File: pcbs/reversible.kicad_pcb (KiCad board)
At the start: 2 copper layers, 132.7 x 86.8 mm, 50 parts

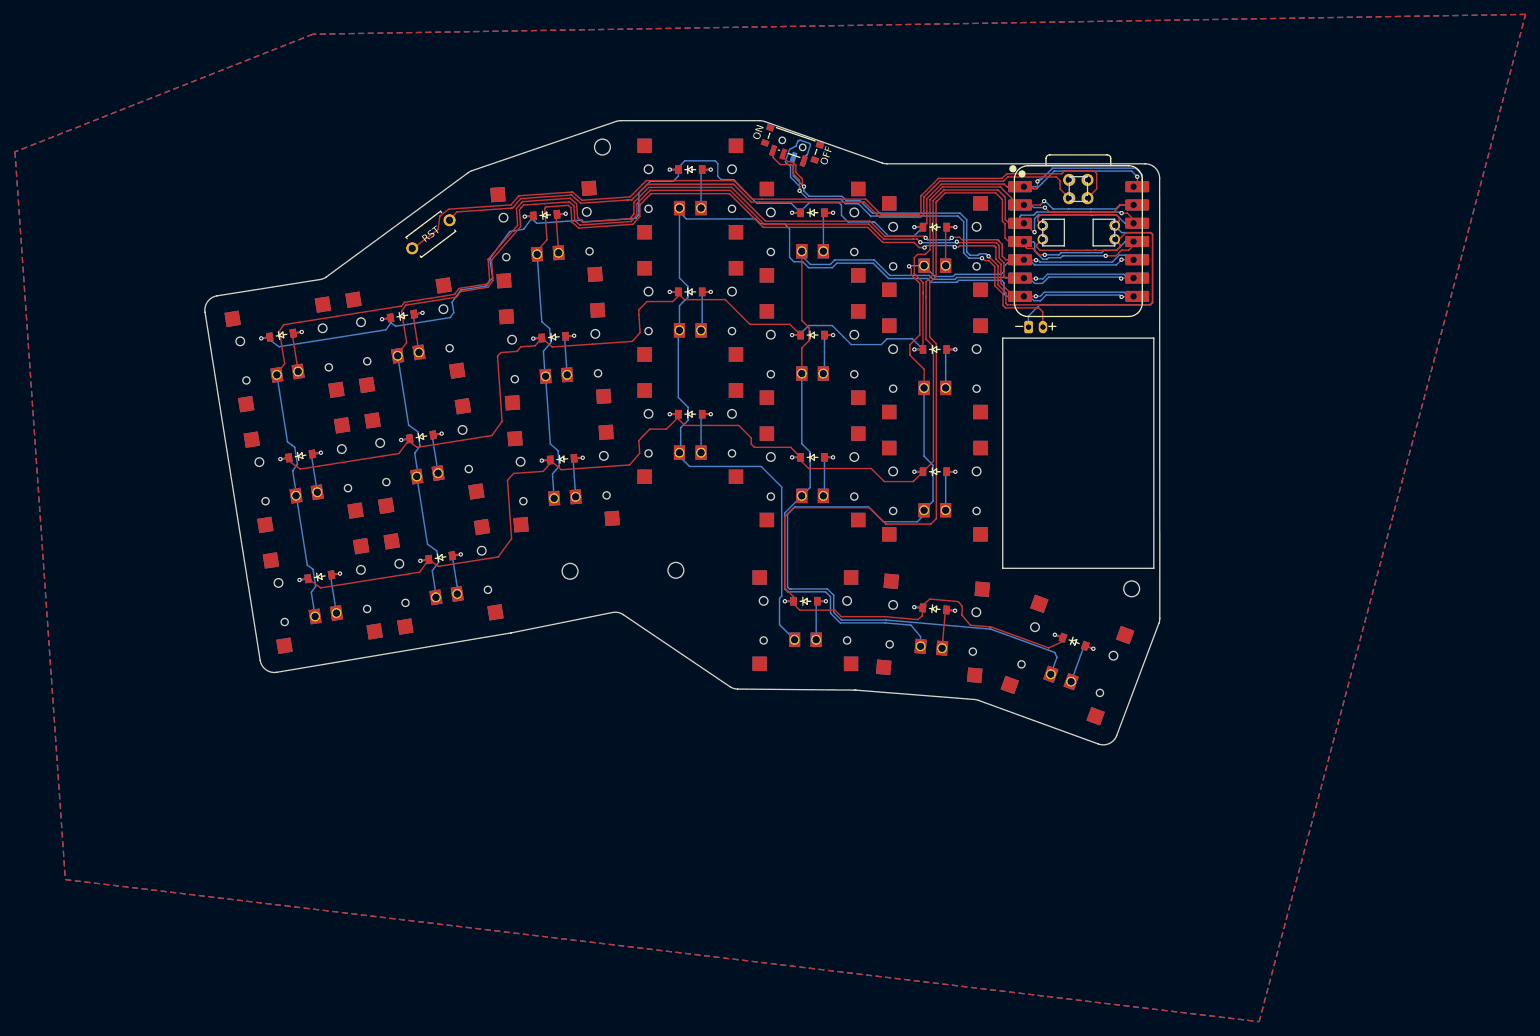
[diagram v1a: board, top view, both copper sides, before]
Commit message: finalized the pcb. cleaned up some tracks. ordered first sample
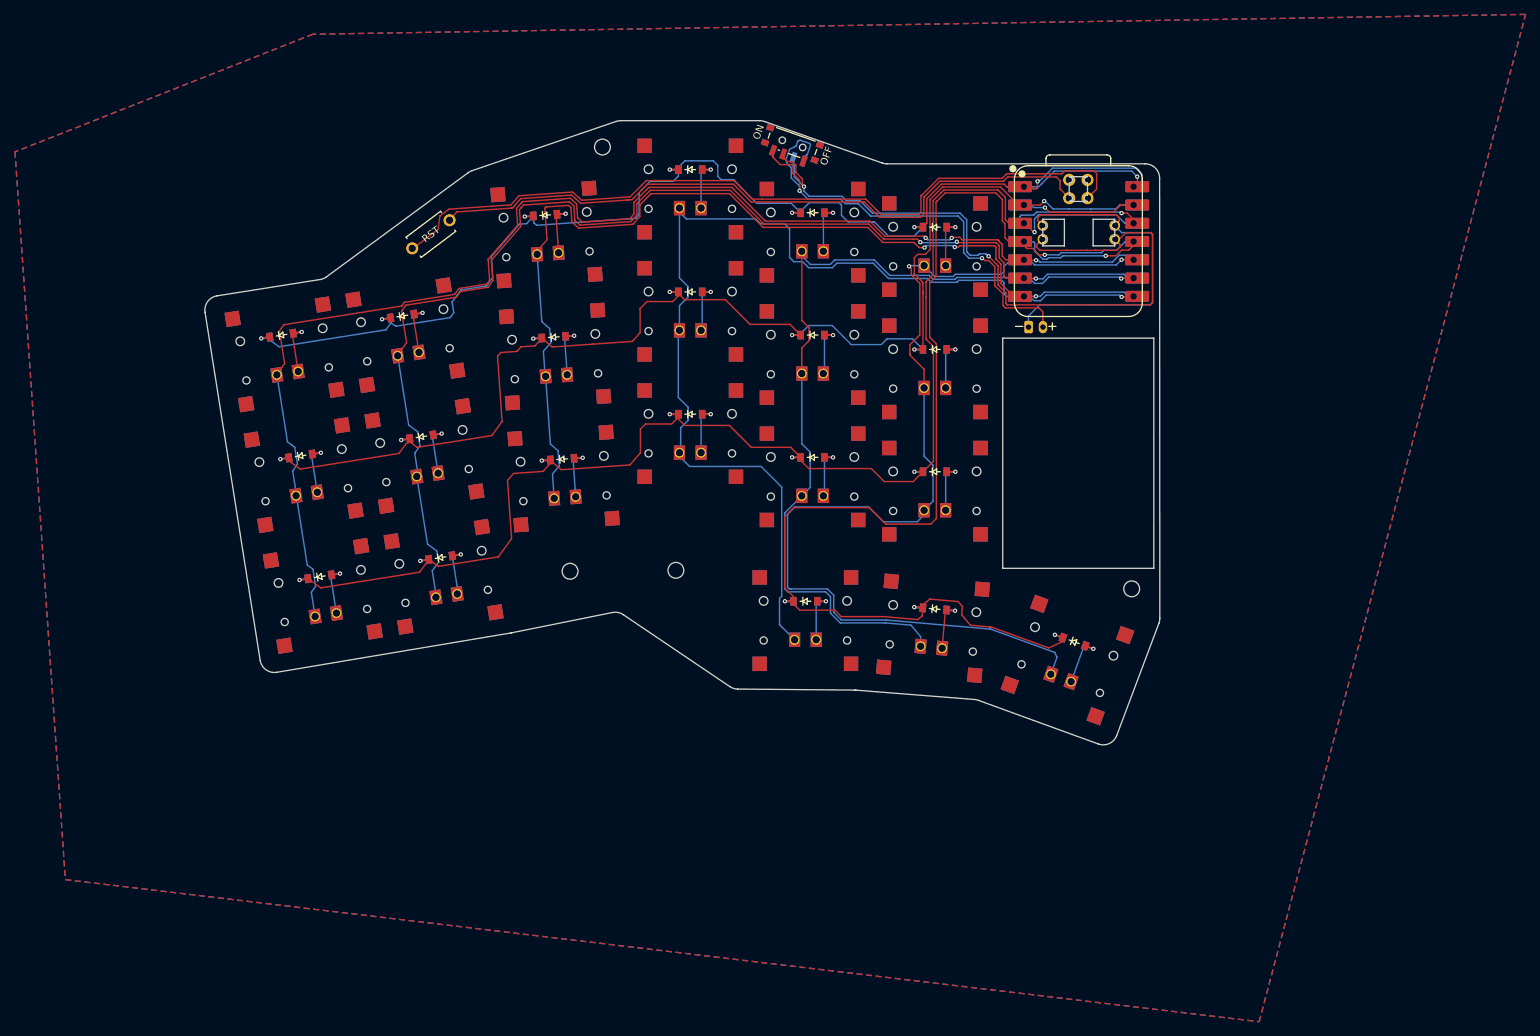
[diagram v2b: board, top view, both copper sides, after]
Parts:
- turned PWR1 to 70.6 degrees
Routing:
- net BAT_P: track 69.5 -> 70.5 mm
- net P9: track 148.0 -> 147.0 mm
- net RAW: track 102.3 -> 103.2 mm

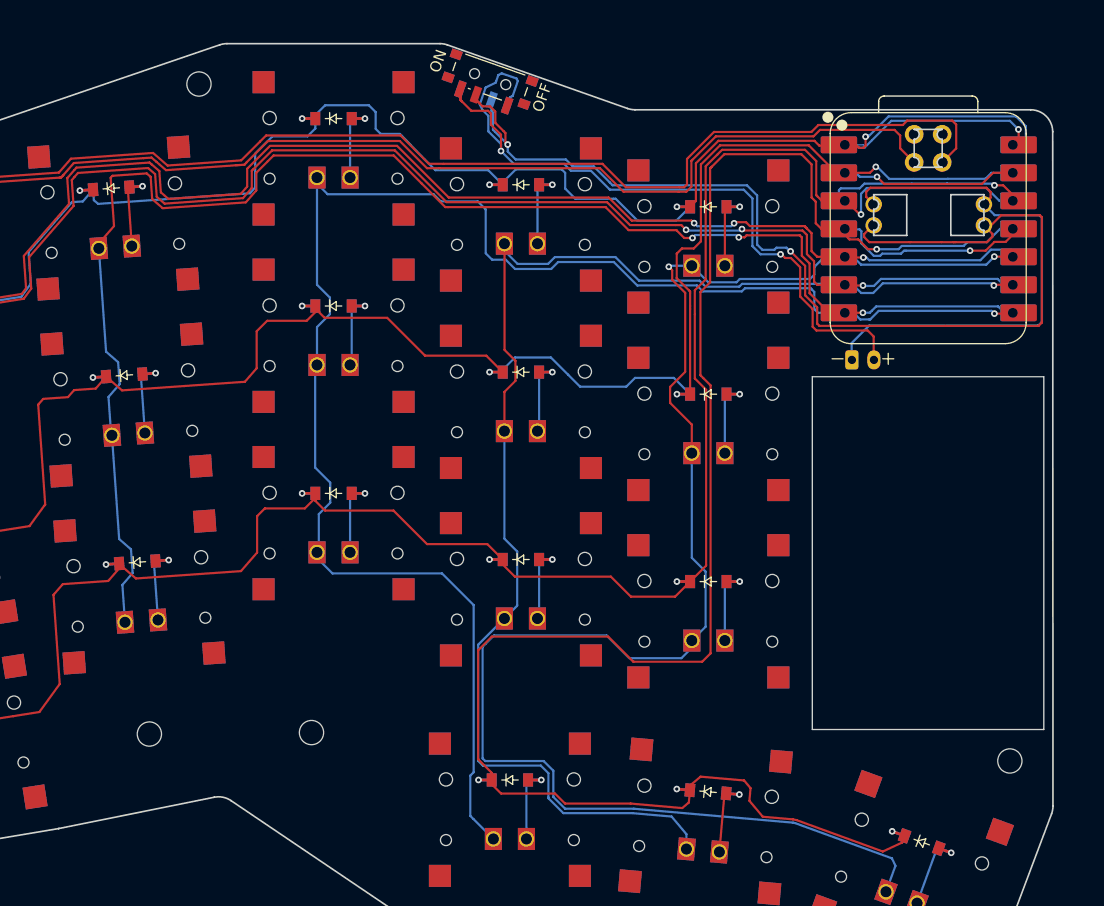
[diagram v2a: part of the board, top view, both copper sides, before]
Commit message: overhauled mcu footprint to meed fab specifications. updated mcu footprint in routed pcb. updated gerbers accordingly. cleaned up custom footprint file for mcu by moving pad to funcion
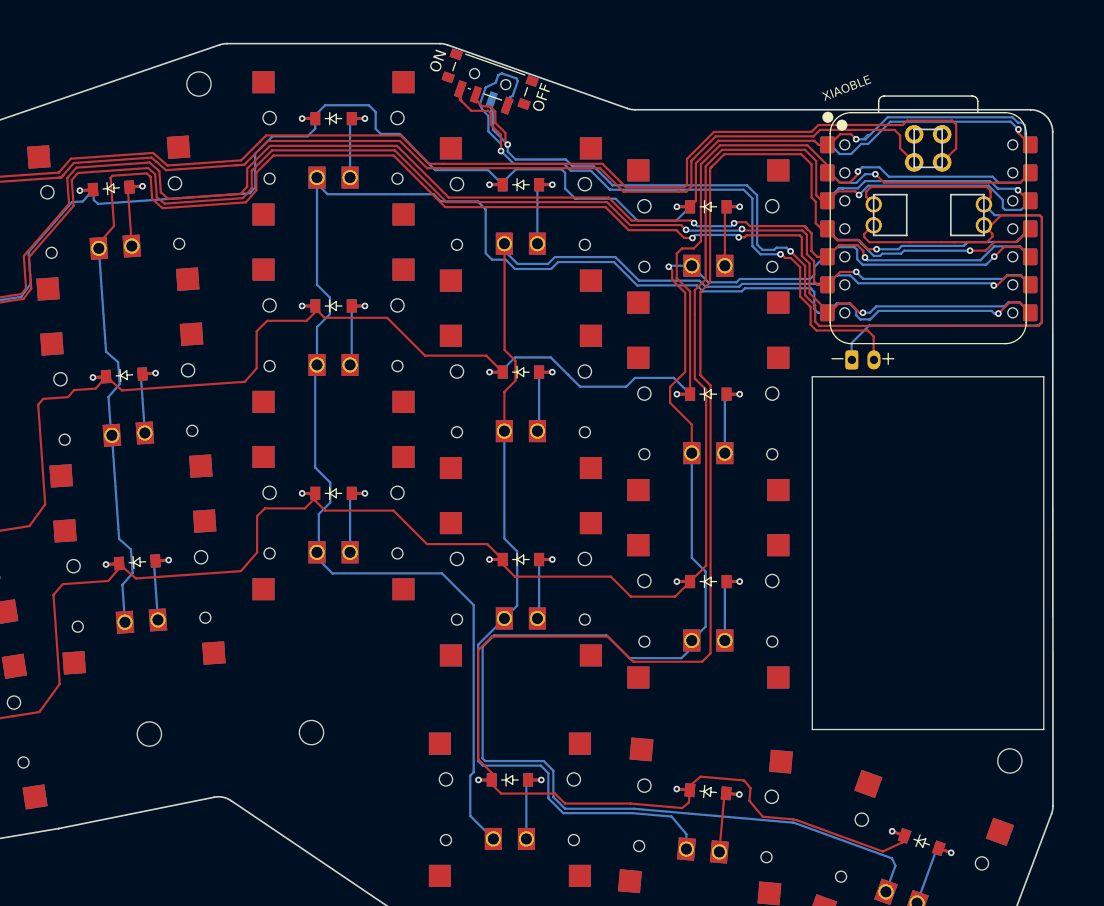
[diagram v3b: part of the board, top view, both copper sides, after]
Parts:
- XIAOBLE: renamed from REF**; footprint XIAO-nRF52840-SMD -> testlibitemkicad:XIAO-nRF52840-SMD-NEW
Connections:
- XIAOBLE pad 10: P9 -> P4
- XIAOBLE pad 11: P10 -> P3
- XIAOBLE pad 12: VCC33 -> P2
- XIAOBLE pad 13: GND -> P1
- XIAOBLE pad 14: VCC5 -> P0
- XIAOBLE pad 8: P7 -> P6
- XIAOBLE pad 9: P8 -> P5
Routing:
- net P7: track 149.3 -> 152.5 mm
- net GND: track 176.4 -> 179.2 mm
- net P9: track 147.0 -> 149.8 mm
- net P1: track 182.9 -> 185.5 mm
- net P4: track 182.7 -> 185.2 mm
- net P6: track 139.5 -> 141.7 mm
- net P5: track 167.1 -> 168.9 mm
- net P8: track 124.1 -> 125.9 mm
- net VCC33: track 18.2 -> 19.8 mm
- net P10: track 19.0 -> 20.5 mm
- net P2: track 199.2 -> 200.0 mm
- net P3: track 167.2 -> 167.8 mm

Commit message: more track cleanup around the mcu. fixed power switch labeling, updated gerbers accordingly
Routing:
- net P0: track 175.2 -> 173.8 mm
- net P7: track 152.5 -> 151.6 mm

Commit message: minor changes to the routing
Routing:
- net RAW: track 103.2 -> 103.9 mm
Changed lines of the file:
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@@
+	)
+	(segment
+		(start 211.806963 48.664056)
+		(end 212.445947 48.664056)
+		(width 0.2)
+		(layer "F.Cu")
+		(net 34)
 	)
 	(segment
@@
 		(width 0.2)
 		(layer "F.Cu")
+		(net 34)
+	)
+	(segment
+		(start 211.80696 48.664059)
+		(end 211.806963 48.664056)
+		(width 0.2)
+		(layer "F.Cu")
